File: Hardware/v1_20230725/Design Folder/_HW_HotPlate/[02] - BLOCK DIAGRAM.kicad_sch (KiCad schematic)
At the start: 0 parts

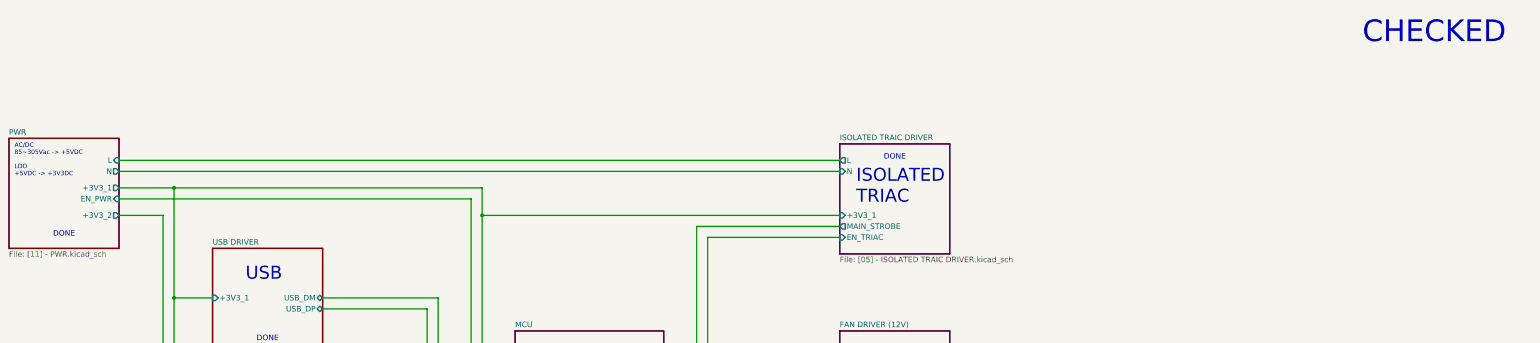
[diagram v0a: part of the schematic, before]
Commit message: Schematic library has been updated
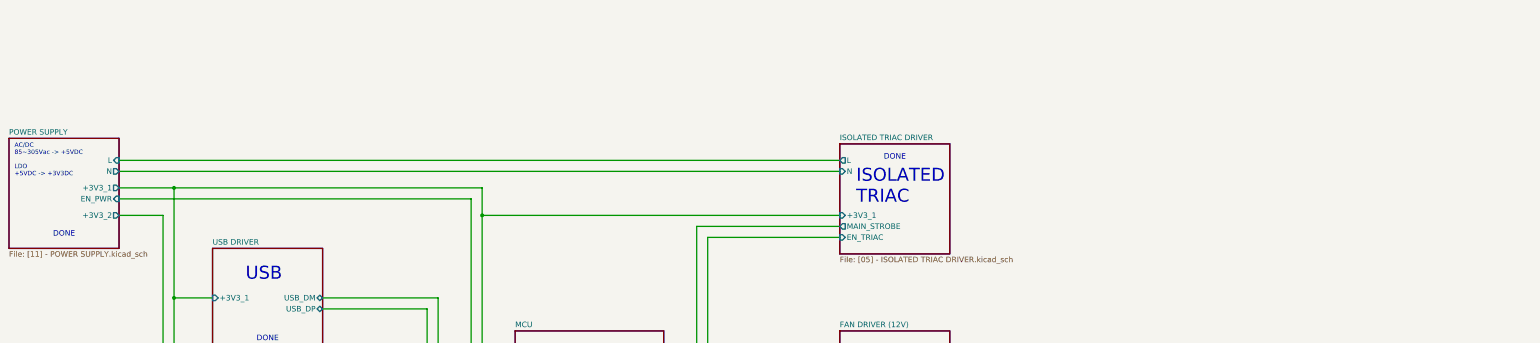
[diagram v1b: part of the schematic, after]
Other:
- sheet ISOLATED TRAIC DRIVER renamed ISOLATED TRIAC DRIVER
- sheet PWR  renamed POWER SUPPLY
- sheet ISOLATED TRIAC DRIVER: file [05] - ISOLATED TRAIC DRIVER.kicad_sch -> [05] - ISOLATED TRIAC DRIVER.kicad_sch
- sheet POWER SUPPLY: file [11] - PWR.kicad_sch -> [11] - POWER SUPPLY.kicad_sch
- note removed: "CHECKED"
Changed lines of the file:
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@@
 (kicad_sch (version 20230121) (generator eeschema)
-  (paper "B")
+  (paper "C")
   (title_block
     (title "Hot Plate")
@@
     (company "Mend0z0")
     (comment 1 "v1")
+    (comment 2 "RELEASED")
     (comment 3 "Siavash Taher Parvar")
     (comment 8 "N/A")
@@
     (effects (font (size 1.016 1.016)) (justify left bottom))
   )
-  (text "CHECKED" (at 382.27 36.83 0)
-    (effects (font (size 5 5)) (justify left bottom))
-  )
   (text "DONE" (at 200.66 139.7 0)
     (effects (font (size 1.27 1.27)) (justify left bottom))
@@
     (stroke (width 0.1524) (type solid))
     (fill (color 0 0 0 0.0000))
-    (property "Sheetname" "PWR " (at 69.85 57.7084 0)
-      (effects (font (size 1.27 1.27)) (justify left bottom))
-    )
-    (property "Sheetfile" "[11] - PWR.kicad_sch" (at 69.85 84.4046 0)
+    (property "Sheetname" "POWER SUPPLY" (at 69.85 57.7084 0)
+      (effects (font (size 1.27 1.27)) (justify left bottom))
+    )
+    (property "Sheetfile" "[11] - POWER SUPPLY.kicad_sch" (at 69.85 84.4046 0)
       (effects (font (size 1.27 1.27)) (justify left top))
     )
@@
     (stroke (width 0.1524) (type solid))
     (fill (color 0 0 0 0.0000))
-    (property "Sheetname" "ISOLATED TRAIC DRIVER" (at 261.62 58.9784 0)
-      (effects (font (size 1.27 1.27)) (justify left bottom))
-    )
-    (property "Sheetfile" "[05] - ISOLATED TRAIC DRIVER.kicad_sch" (at 261.62 85.6746 0)
-      (effects (font (size 1.27 1.27)) (justify left top))
-    )
+    (property "Sheetname" "ISOLATED TRIAC DRIVER" (at 261.62 58.9784 0)
+      (effects (font (size 1.27 1.27)) (justify left bottom))
+    )
+    (property "Sheetfile" "[05] - ISOLATED TRIAC DRIVER.kicad_sch" (at 261.62 85.6746 0)
+      (effects (font (size 1.27 1.27)) (justify left top))
+    )

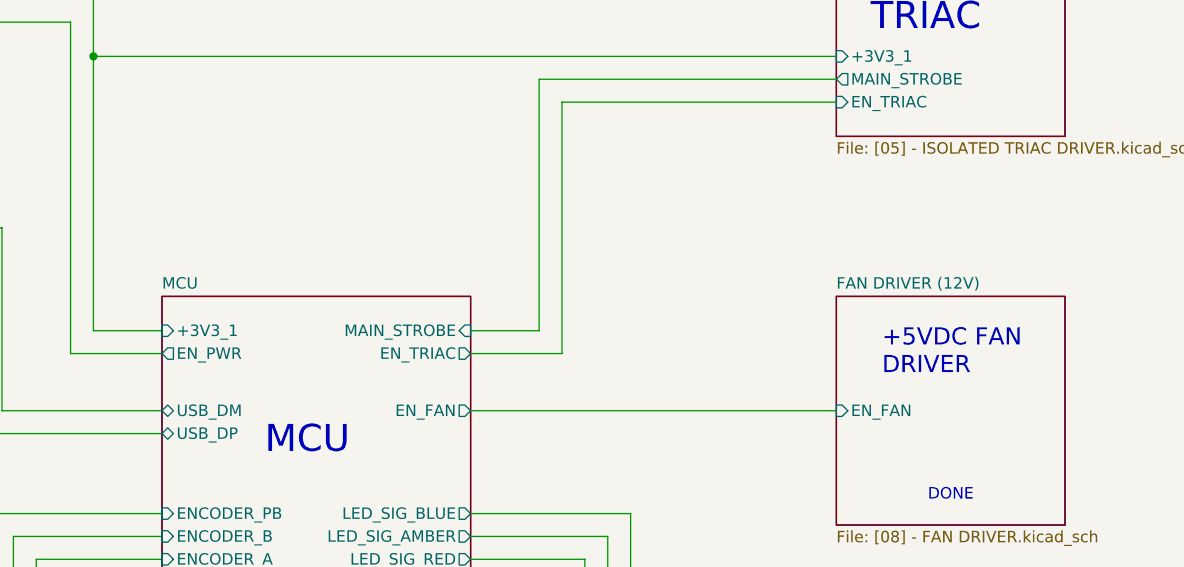
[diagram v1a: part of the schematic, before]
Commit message: components have been updated
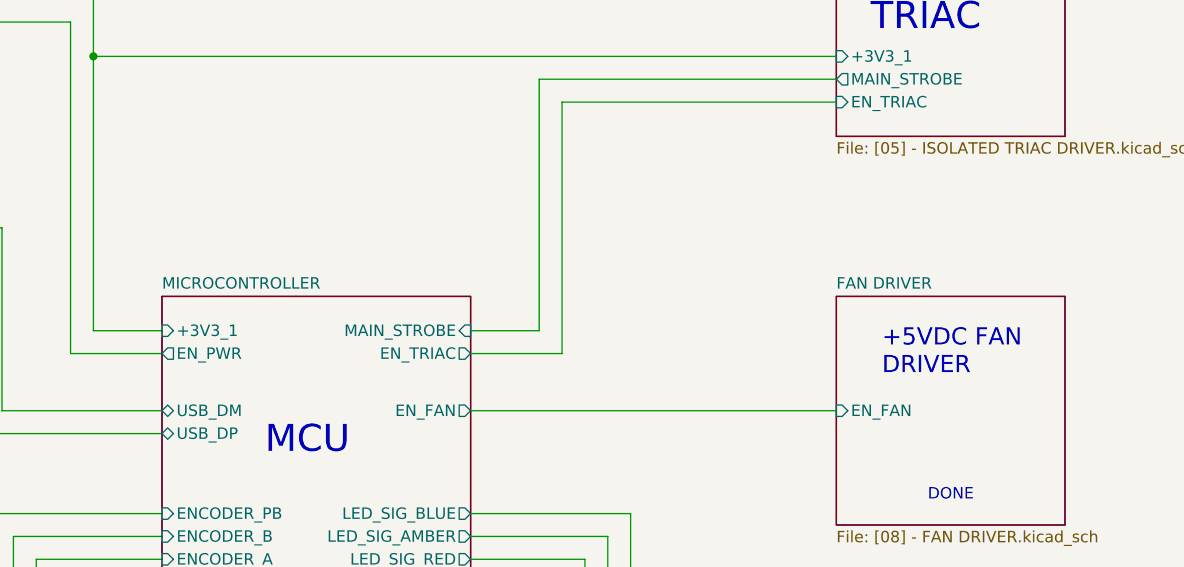
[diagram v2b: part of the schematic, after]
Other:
- sheet FAN DRIVER (12V) renamed FAN DRIVER
- sheet MCU renamed MICROCONTROLLER
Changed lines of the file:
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@@
     (stroke (width 0.1524) (type solid))
     (fill (color 0 0 0 0.0000))
-    (property "Sheetname" "FAN DRIVER (12V)" (at 261.62 102.1584 0)
+    (property "Sheetname" "FAN DRIVER" (at 261.62 102.1584 0)
       (effects (font (size 1.27 1.27)) (justify left bottom))
     )
@@
     (stroke (width 0.1524) (type solid))
     (fill (color 0 0 0 0.0000))
-    (property "Sheetname" "MCU" (at 186.69 102.1584 0)
+    (property "Sheetname" "MICROCONTROLLER" (at 186.69 102.1584 0)
       (effects (font (size 1.27 1.27)) (justify left bottom))
     )
